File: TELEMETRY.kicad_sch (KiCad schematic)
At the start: 1 part

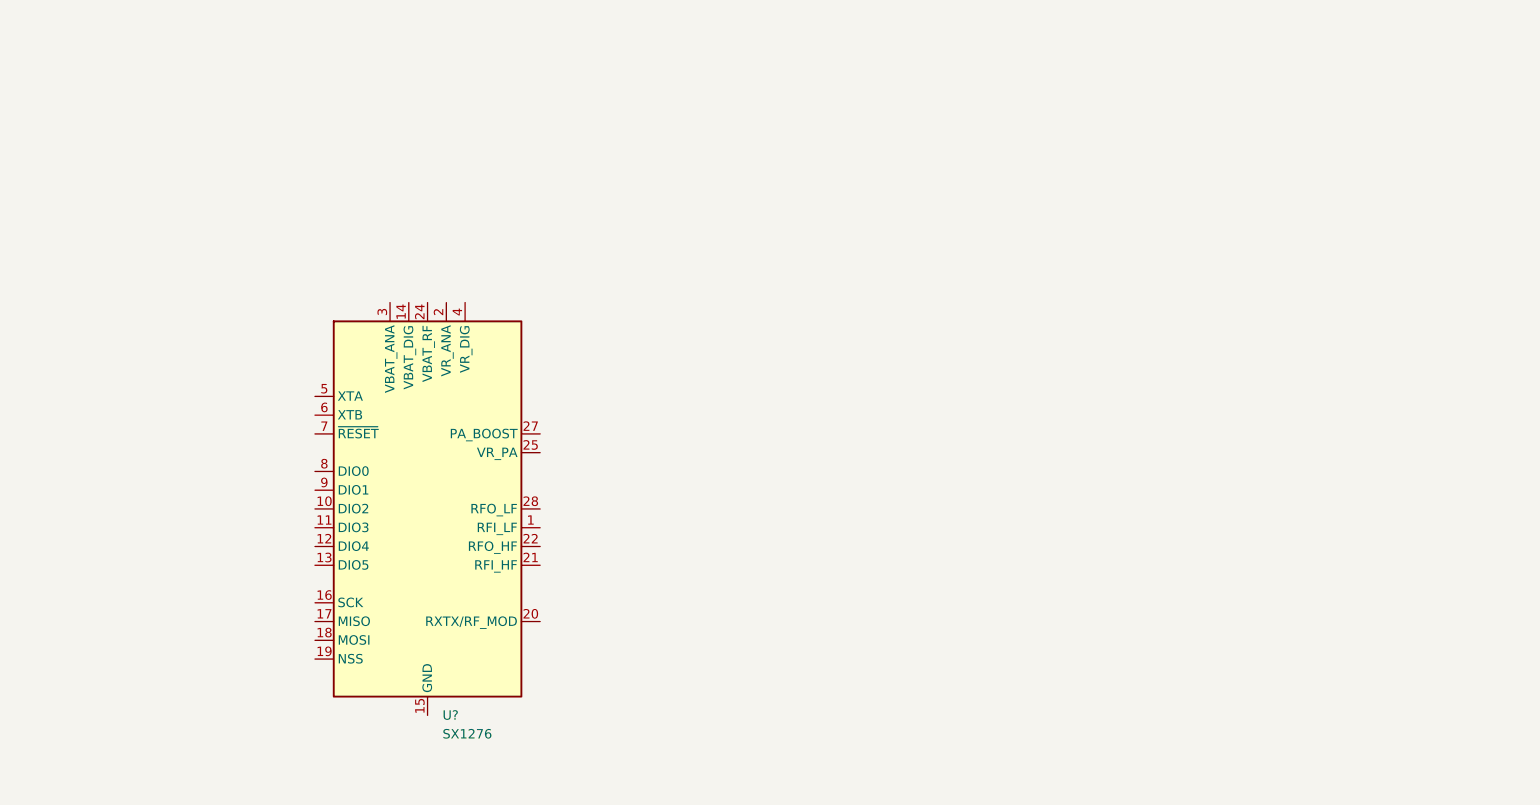
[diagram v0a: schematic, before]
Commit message: finished telemetry
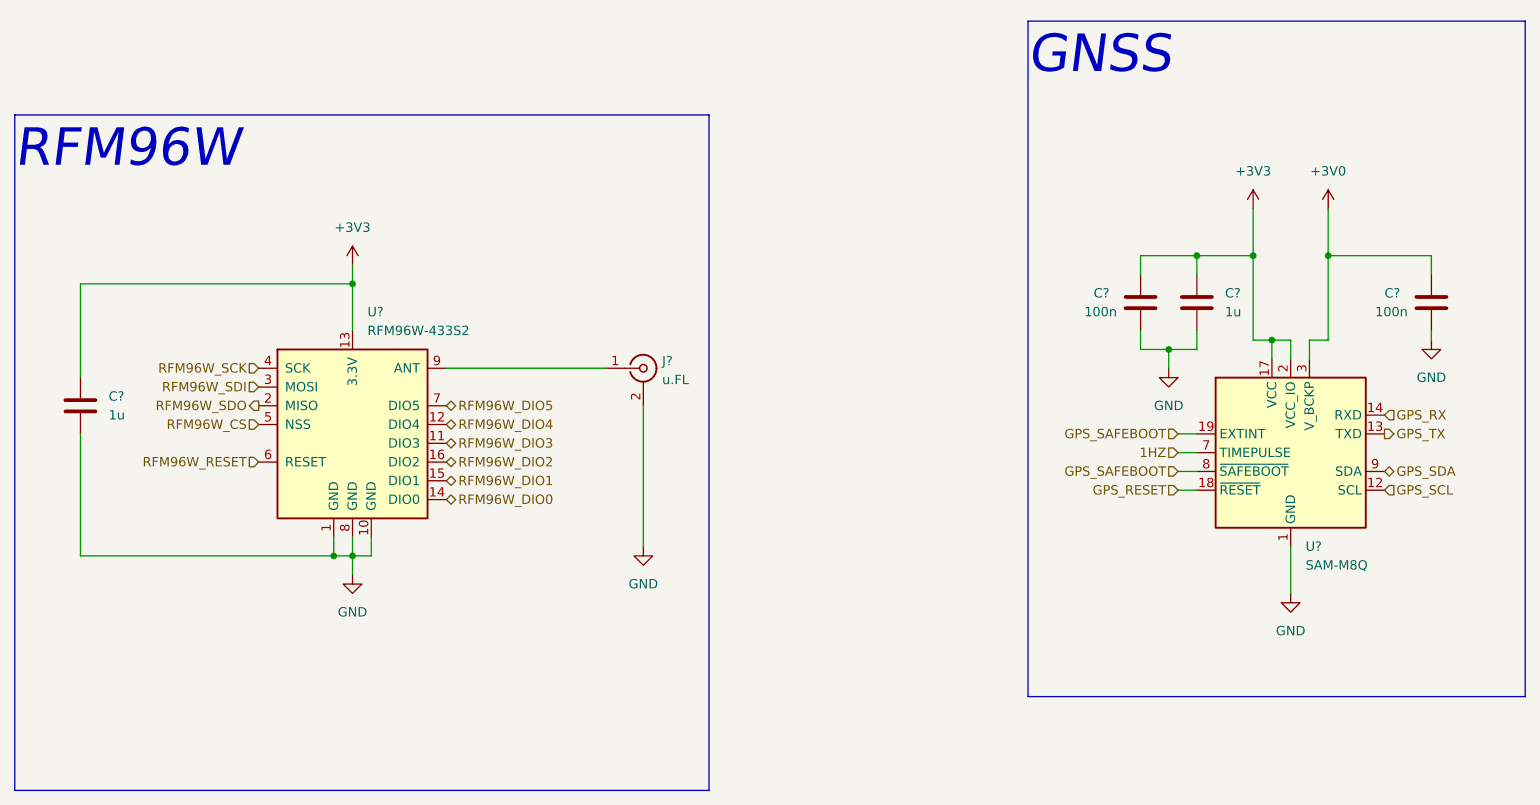
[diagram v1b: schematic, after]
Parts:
- removed U?: SX1276, Package_DFN_QFN:QFN-28-1EP_6x6mm_P0.65mm_EP4.8x4.8mm, symbol RF:SX1276
- added C? (x2): 1u, Capacitor_SMD:C_0805_2012Metric, symbol Device:C
- added C? (x2): 100n, Capacitor_SMD:C_0805_2012Metric, symbol Device:C
- added J?: u.FL, Connector_Coaxial:U.FL_Hirose_U.FL-R-SMT-1_Vertical, symbol Connector:Conn_Coaxial
- added U?: SAM-M8Q, RF_GPS:ublox_SAM-M8Q, symbol RF_GPS:SAM-M8Q
- added U?: RFM96W-433S2, symbol RF_Module:RFM96W-433S2
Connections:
- new net: J?.1 (In), U?.9 (ANT)
- new net +3V0: C?.1, U?.3 (V_BCKP)
- new net +3V3: C?.1, C?.1, C?.2, U?.13 (3.3V), U?.17 (VCC), U?.2 (VCC_IO)
- new net 1HZ: U?.7 (TIMEPULSE)
- new net GND: C?.1, C?.2, C?.2, C?.2, J?.2 (Ext), U?.1 (GND), U?.1 (GND), U?.10 (GND), U?.10 (GND), U?.11 (GND), U?.15 (GND), U?.16 (GND), U?.20 (GND), U?.4 (GND), U?.5 (GND), U?.6 (GND), U?.8 (GND)
- new net GPS_RESET: U?.18 (~{RESET})
- new net GPS_RX: U?.14 (RXD)
- new net GPS_SAFEBOOT: U?.19 (EXTINT), U?.8 (~{SAFEBOOT})
- new net GPS_SCL: U?.12 (SCL)
- new net GPS_SDA: U?.9 (SDA)
- new net GPS_TX: U?.13 (TXD)
- new net RFM96W_CS: U?.5 (NSS)
- new net RFM96W_DIO0: U?.14 (DIO0)
- new net RFM96W_DIO1: U?.15 (DIO1)
- new net RFM96W_DIO2: U?.16 (DIO2)
- new net RFM96W_DIO3: U?.11 (DIO3)
- new net RFM96W_DIO4: U?.12 (DIO4)
- new net RFM96W_DIO5: U?.7 (DIO5)
- new net RFM96W_RESET: U?.6 (RESET)
- new net RFM96W_SCK: U?.4 (SCK)
- new net RFM96W_SDI: U?.3 (MOSI)
- new net RFM96W_SDO: U?.2 (MISO)
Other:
- note added: "GNSS"
- note added: "RFM96W"
